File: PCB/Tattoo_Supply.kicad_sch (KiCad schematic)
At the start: 1 part

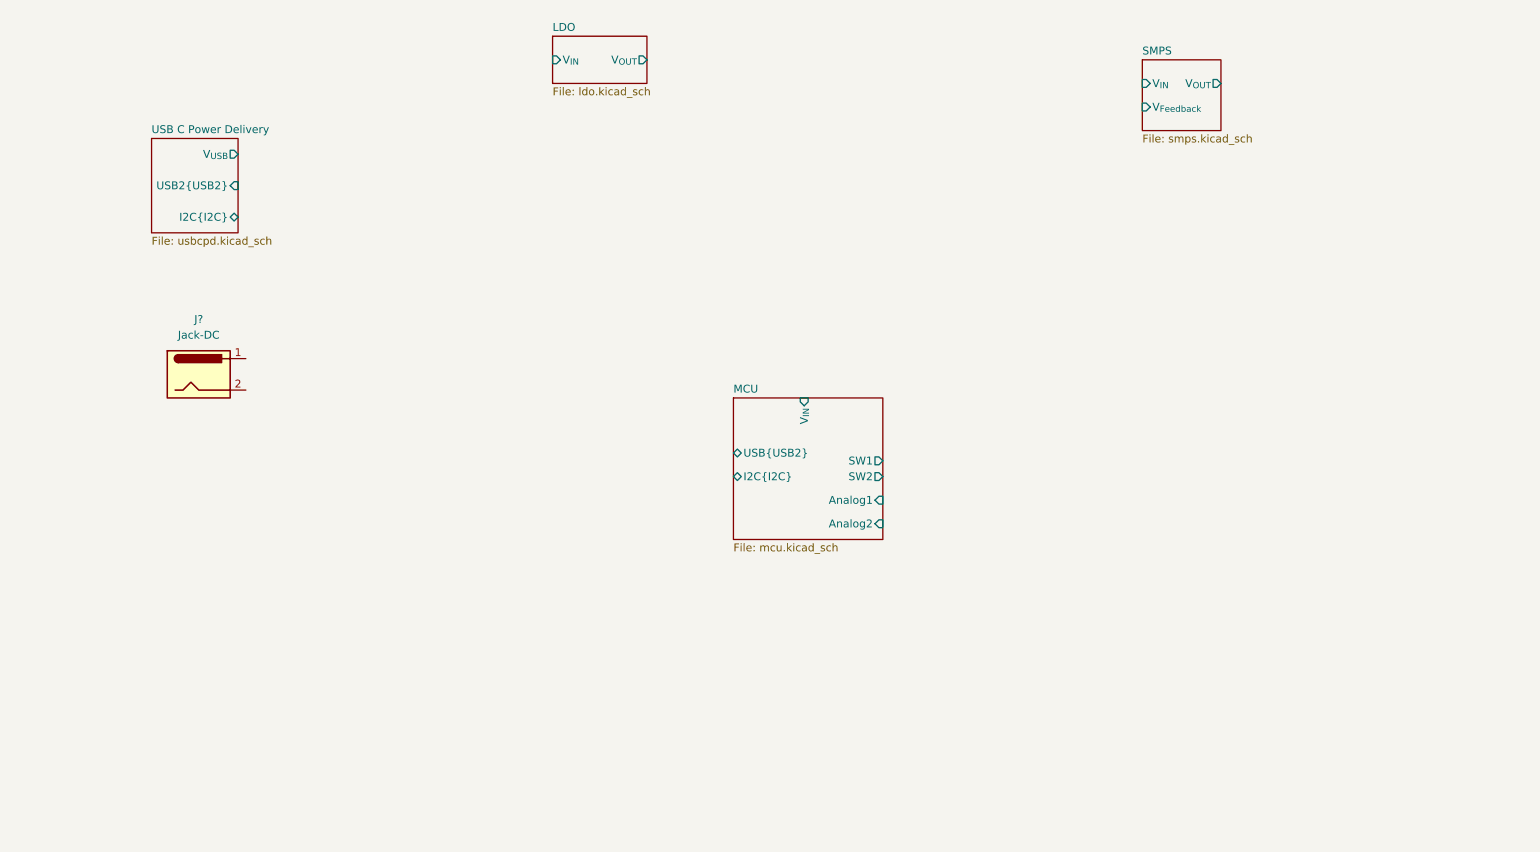
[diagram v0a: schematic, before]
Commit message: ok dcdc and power switches
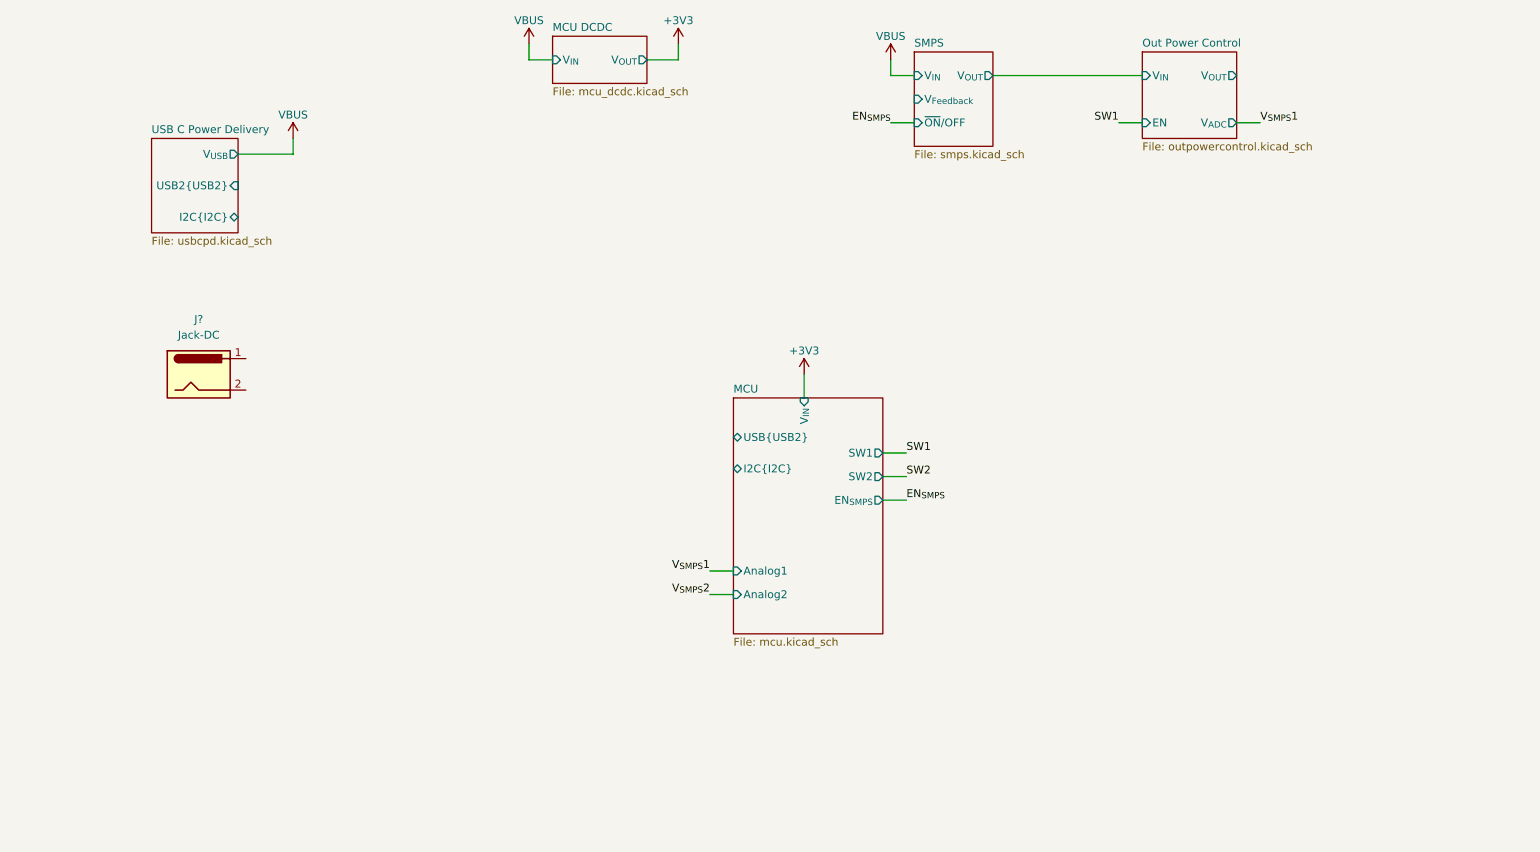
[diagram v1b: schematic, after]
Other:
- removed sheet LDO
- added sheet MCU DCDC (mcu_dcdc.kicad_sch)
- added sheet Out Power Control (outpowercontrol.kicad_sch)
- sheet MCU ports: added EN_{SMPS}; removed none
- sheet SMPS ports: added ~{ON}/OFF; removed none

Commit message: add dac
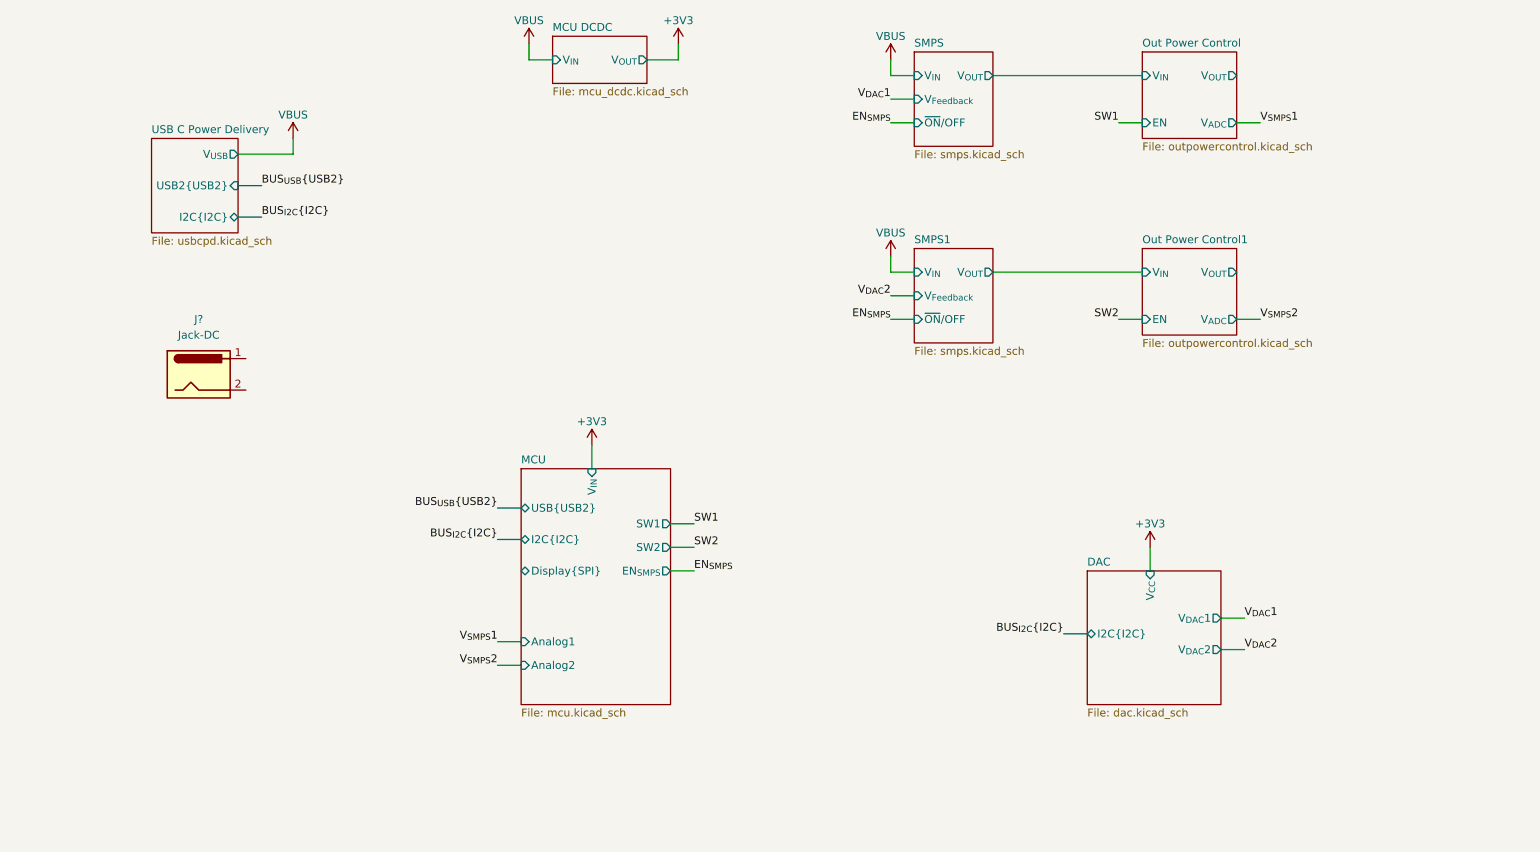
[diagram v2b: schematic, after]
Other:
- added sheet DAC (dac.kicad_sch)
- added sheet Out Power Control1 (outpowercontrol.kicad_sch)
- added sheet SMPS1 (smps.kicad_sch)
- sheet MCU ports: added Display{SPI}; removed none

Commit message: done with sch before ERC and footprints
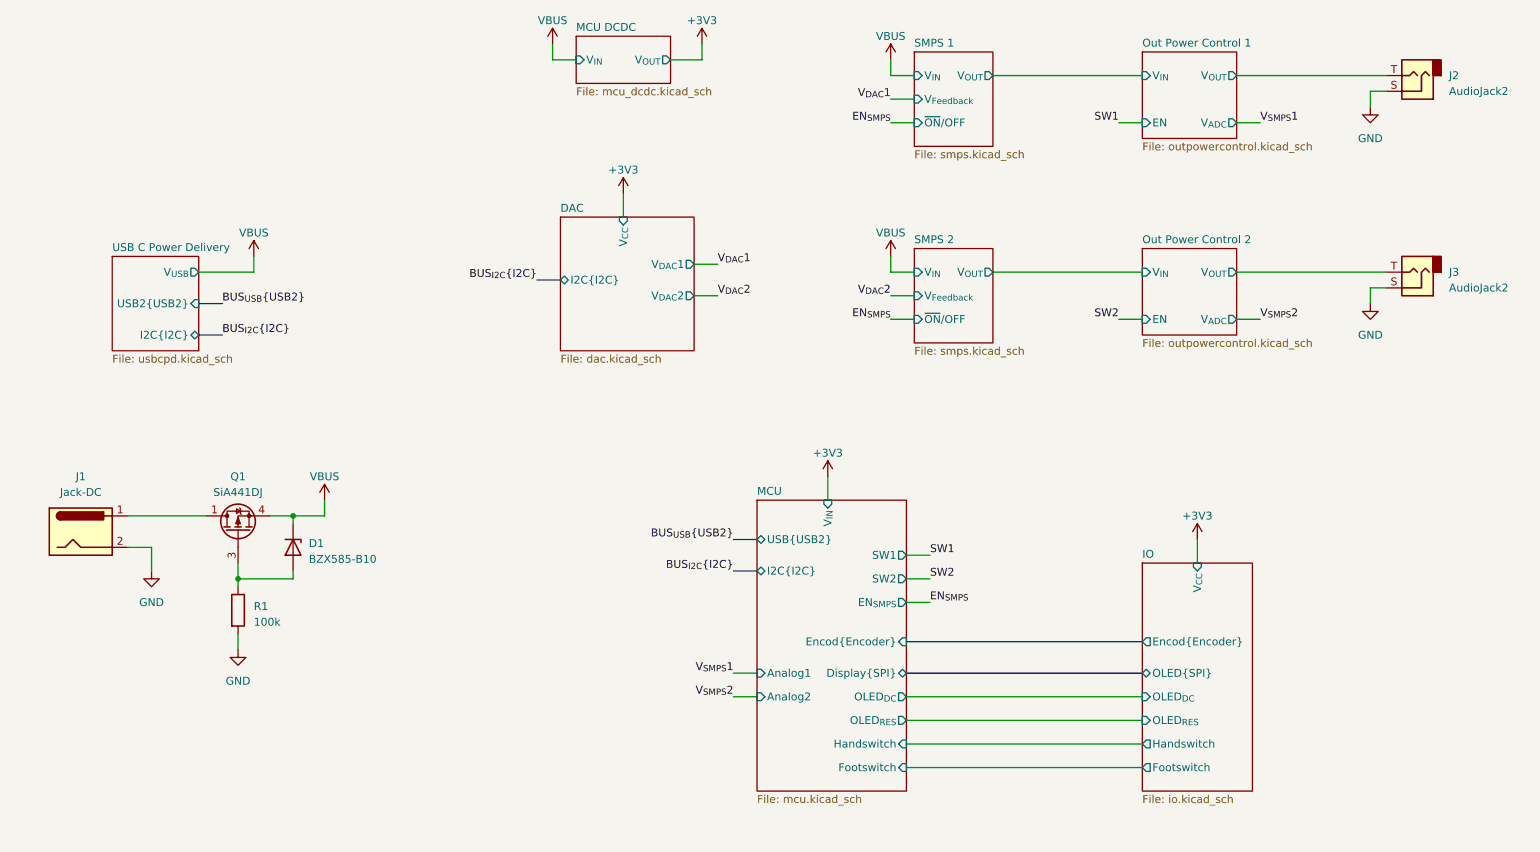
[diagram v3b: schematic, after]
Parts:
- added D1: BZX585-B10, Diode_SMD:D_SOD-523, symbol Device:D_Zener
- added J2, J3: AudioJack2, symbol Connector_Audio:AudioJack2
- added Q1: SiA441DJ, Package_TO_SOT_SMD:Vishay_PowerPAK_SC70-6L_Single, symbol Transistor_FET:SiA449DJ
- added R1: 100k, symbol Device:R
- gave numbers to parts that had none: 1
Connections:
- net Out Power Control 1/V_{OUT}: now also J2.T
- net Out Power Control 2/V_{OUT}: now also J3.T
- net VBUS: now also D1.1 (K), Q1.4 (S)
- net at J1.1: now also Q1.1 (D)
- net GND: now reaches J1.2
- net GND: now also J2.S, J3.S, R1.2
- new net: D1.2 (A), Q1.3 (G), R1.1
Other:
- sheet Out Power Control renamed Out Power Control 1
- sheet Out Power Control1 renamed Out Power Control 2
- sheet SMPS renamed SMPS 1
- sheet SMPS1 renamed SMPS 2
- added sheet IO (io.kicad_sch)
- sheet MCU ports: added Encod{Encoder}, Footswitch, Handswitch, OLED_{DC}, OLED_{RES}; removed none
- title: (none) -> Tattoo Power Supply
- moved on the sheet: J1

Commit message: begin BOM
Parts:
- D1: MPN (none) -> BZX585-B10,135; Manufacturer (none) -> Nexperia
- Q1: MPN (none) -> SIA441DJ-T1-GE3; Manufacturer (none) -> Vishay Semiconductors
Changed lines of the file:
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@@
     (rev "V1.0")
   )
-  (bus_alias "I2C" (members "SDA" "SCL"))
-  (bus_alias "Encoder" (members "DT" "CLK" "SW"))
+  (bus_alias "SPI" (members "~{CS}" "SCK" "MOSI" "MISO"))
   (bus_alias "USB2" (members "D+" "D-"))
   (bus_alias "UART" (members "Tx" "Rx"))
-  (bus_alias "SPI" (members "~{CS}" "SCK" "MOSI" "MISO"))
+  (bus_alias "Encoder" (members "DT" "CLK" "SW"))
+  (bus_alias "I2C" (members "SDA" "SCL"))
   (junction (at 60.96 124.46) (diameter 0) (color 0 0 0 0)
   )
@@
       (effects (font (size 1.27 1.27)) hide)
     )
+    (property "MPN" "" (at 251.46 43.18 0)
+      (effects (font (size 1.27 1.27)) hide)
+    )
+    (property "Manufacturer" "" (at 251.46 43.18 0)
+      (effects (font (size 1.27 1.27)) hide)
+    )
     (pin "S")
     (pin "T")
@@
       (effects (font (size 1.27 1.27)) hide)
     )
+    (property "MPN" "BZX585-B10,135" (at 69.85 119.38 0)
+      (effects (font (size 1.27 1.27)) hide)
+    )
+    (property "Manufacturer" "Nexperia" (at 69.85 119.38 0)
+      (effects (font (size 1.27 1.27)) hide)
+    )
     (pin "1")
     (pin "2")
@@
       (effects (font (size 1.27 1.27)) hide)
     )
+    (property "MPN" "" (at 251.46 74.93 0)
+      (effects (font (size 1.27 1.27)) hide)
+    )
+    (property "Manufacturer" "" (at 251.46 74.93 0)
+      (effects (font (size 1.27 1.27)) hide)
+    )
     (pin "S")
     (pin "T")
@@
       (effects (font (size 1.27 1.27)) hide)
     )
+    (property "MPN" "" (at 35.56 116.84 0)
+      (effects (font (size 1.27 1.27)) hide)
+    )
+    (property "Manufacturer" "" (at 35.56 116.84 0)
+      (effects (font (size 1.27 1.27)) hide)
+    )
     (pin "1")
     (pin "2")
@@
       (effects (font (size 1.27 1.27)) (justify left) hide)
     )
+    (property "MPN" "SIA441DJ-T1-GE3" (at 60.96 116.84 0)
+      (effects (font (size 1.27 1.27)) hide)
+    )
+    (property "Manufacturer" "Vishay Semiconductors" (at 60.96 116.84 0)
+      (effects (font (size 1.27 1.27)) hide)
+    )
     (pin "1")
     (pin "3")
@@
       (effects (font (size 1.27 1.27)) hide)
     )
+    (property "MPN" "" (at 60.96 129.54 0)
+      (effects (font (size 1.27 1.27)) hide)
+    )
+    (property "Manufacturer" "" (at 60.96 129.54 0)
+      (effects (font (size 1.27 1.27)) hide)
+    )

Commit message: Resistors ok in BOM
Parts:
- R1: footprint (none) -> Resistor_SMD:R_0603_1608Metric; MPN (none) -> ERJ-3EKF1003V; Manufacturer (none) -> Panasonic
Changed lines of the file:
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@@
     (rev "V1.0")
   )
+  (bus_alias "UART" (members "Tx" "Rx"))
+  (bus_alias "I2C" (members "SDA" "SCL"))
+  (bus_alias "Encoder" (members "DT" "CLK" "SW"))
+  (bus_alias "USB2" (members "D+" "D-"))
   (bus_alias "SPI" (members "~{CS}" "SCK" "MOSI" "MISO"))
-  (bus_alias "USB2" (members "D+" "D-"))
-  (bus_alias "UART" (members "Tx" "Rx"))
-  (bus_alias "Encoder" (members "DT" "CLK" "SW"))
-  (bus_alias "I2C" (members "SDA" "SCL"))
   (junction (at 60.96 124.46) (diameter 0) (color 0 0 0 0)
   )
@@
       (effects (font (size 1.27 1.27)) (justify left))
     )
-    (property "Footprint" "" (at 59.182 129.54 90)
+    (property "Footprint" "Resistor_SMD:R_0603_1608Metric" (at 59.182 129.54 90)
       (effects (font (size 1.27 1.27)) hide)
     )
@@
       (effects (font (size 1.27 1.27)) hide)
     )
-    (property "MPN" "" (at 60.96 129.54 0)
-      (effects (font (size 1.27 1.27)) hide)
-    )
-    (property "Manufacturer" "" (at 60.96 129.54 0)
-      (effects (font (size 1.27 1.27)) hide)
-    )
+    (property "MPN" "ERJ-3EKF1003V" (at 60.96 129.54 0)
+      (effects (font (size 1.27 1.27)) hide)
+    )
+    (property "Manufacturer" "Panasonic" (at 60.96 129.54 0)
+      (effects (font (size 1.27 1.27)) hide)
+    )

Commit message: bom almost finished
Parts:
- removed J1: Jack-DC, symbol Connector:Jack-DC
- added J1: Barrel_Jack_Switch, Connector_BarrelJack:BarrelJack_CUI_PJ-102AH_Horizontal, symbol Connector:Barrel_Jack_Switch
- J2: value AudioJack2 -> Out_{1}; MPN (none) -> MJ-63022A; Manufacturer (none) -> CUI Devices
- J3: value AudioJack2 -> Out_{2}; MPN (none) -> MJ-63022A; Manufacturer (none) -> CUI Devices
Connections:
- net GND: now also J1.2, J1.3
- net at Q1.1 (D): now also J1.1
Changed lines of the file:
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@@
     (rev "V1.0")
   )
+  (bus_alias "USB2" (members "D+" "D-"))
+  (bus_alias "SPI" (members "~{CS}" "SCK" "MOSI" "MISO"))
+  (bus_alias "Encoder" (members "DT" "CLK" "SW"))
   (bus_alias "UART" (members "Tx" "Rx"))
   (bus_alias "I2C" (members "SDA" "SCL"))
-  (bus_alias "Encoder" (members "DT" "CLK" "SW"))
-  (bus_alias "USB2" (members "D+" "D-"))
-  (bus_alias "SPI" (members "~{CS}" "SCK" "MOSI" "MISO"))
+  (junction (at 46.99 119.38) (diameter 0) (color 0 0 0 0)
+  )
   (junction (at 60.96 124.46) (diameter 0) (color 0 0 0 0)
   )
@@
     (stroke (width 0) (type default))
   )
+  (wire (pts (xy 46.99 116.84) (xy 46.99 119.38))
+    (stroke (width 0) (type default))
+  )
   (wire (pts (xy 168.91 120.65) (xy 172.72 120.65))
     (stroke (width 0) (type default))
@@
     (stroke (width 0) (type default))
   )
+  (wire (pts (xy 43.18 116.84) (xy 46.99 116.84))
+    (stroke (width 0) (type default))
+  )
   (wire (pts (xy 166.37 40.64) (xy 166.37 43.18))
     (stroke (width 0) (type default))
@@
   )
   (symbol (lib_id "Connector_Audio:AudioJack2") (at 251.46 43.18 180) (unit 1)
-    (in_bom yes) (on_board yes) (dnp no) (fields_autoplaced)
+    (in_bom yes) (on_board yes) (dnp no)
     (property "Reference" "J2" (at 256.54 43.18 0)
       (effects (font (size 1.27 1.27)) (justify right))
     )
-    (property "Value" "AudioJack2" (at 256.54 45.72 0)
+    (property "Value" "Out_{1}" (at 256.54 45.72 0)
       (effects (font (size 1.27 1.27)) (justify right))
     )
@@
       (effects (font (size 1.27 1.27)) hide)
     )
-    (property "MPN" "" (at 251.46 43.18 0)
-      (effects (font (size 1.27 1.27)) hide)
-    )
-    (property "Manufacturer" "" (at 251.46 43.18 0)
+    (property "MPN" "MJ-63022A" (at 251.46 43.18 0)
+      (effects (font (size 1.27 1.27)) hide)
+    )
+    (property "Manufacturer" "CUI Devices" (at 251.46 43.18 0)
       (effects (font (size 1.27 1.27)) hide)
     )
@@
   )
   (symbol (lib_id "Connector_Audio:AudioJack2") (at 251.46 74.93 180) (unit 1)
-    (in_bom yes) (on_board yes) (dnp no) (fields_autoplaced)
+    (in_bom yes) (on_board yes) (dnp no)
     (property "Reference" "J3" (at 256.54 74.93 0)
       (effects (font (size 1.27 1.27)) (justify right))
     )
-    (property "Value" "AudioJack2" (at 256.54 77.47 0)
+    (property "Value" "Out_{2}" (at 256.54 77.47 0)
       (effects (font (size 1.27 1.27)) (justify right))
     )
@@
       (effects (font (size 1.27 1.27)) hide)
     )
-    (property "MPN" "" (at 251.46 74.93 0)
-      (effects (font (size 1.27 1.27)) hide)
-    )
-    (property "Manufacturer" "" (at 251.46 74.93 0)
+    (property "MPN" "MJ-63022A" (at 251.46 74.93 0)
+      (effects (font (size 1.27 1.27)) hide)
+    )
+    (property "Manufacturer" "CUI Devices" (at 251.46 74.93 0)
       (effects (font (size 1.27 1.27)) hide)
     )
@@
     )
   )
-  (symbol (lib_id "Connector:Jack-DC") (at 35.56 116.84 0) (unit 1)
-    (in_bom yes) (on_board yes) (dnp no) (fields_autoplaced)
-    (property "Reference" "J1" (at 35.56 107.95 0)
-      (effects (font (size 1.27 1.27)))
-    )
-    (property "Value" "Jack-DC" (at 35.56 110.49 0)
-      (effects (font (size 1.27 1.27)))
-    )
-    (property "Footprint" "" (at 36.83 117.856 0)
+  (symbol (lib_id "power:VBUS") (at 166.37 72.39 0) (unit 1)
+    (in_bom yes) (on_board yes) (dnp no) (fields_autoplaced)
+    (property "Reference" "#PWR010" (at 166.37 76.2 0)
+      (effects (font (size 1.27 1.27)) hide)
+    )
+    (property "Value" "VBUS" (at 166.37 68.58 0)
+      (effects (font (size 1.27 1.27)))
+    )
+    (property "Footprint" "" (at 166.37 72.39 0)
+      (effects (font (size 1.27 1.27)) hide)
+    )
+    (property "Datasheet" "" (at 166.37 72.39 0)
+      (effects (font (size 1.27 1.27)) hide)
+    )
+    (pin "1")
+    (instances
+      (project "Tattoo_Supply"
+        (path "/036b57f3-323c-4da7-bad2-1c27fa1415e1"
+          (reference "#PWR010") (unit 1)
+        )
+      )
+    )
+  )
+  (symbol (lib_id "Connector:Barrel_Jack_Switch") (at 35.56 116.84 0) (unit 1)
+    (in_bom yes) (on_board yes) (dnp no) (fields_autoplaced)
+    (property "Reference" "J1" (at 35.56 109.22 0)
+      (effects (font (size 1.27 1.27)))
+    )
+    (property "Value" "Barrel_Jack_Switch" (at 35.56 111.76 0)
+      (effects (font (size 1.27 1.27)))
+    )
+    (property "Footprint" "Connector_BarrelJack:BarrelJack_CUI_PJ-102AH_Horizontal" (at 36.83 117.856 0)
       (effects (font (size 1.27 1.27)) hide)
     )
@@
       (effects (font (size 1.27 1.27)) hide)
     )
-    (property "MPN" "" (at 35.56 116.84 0)
-      (effects (font (size 1.27 1.27)) hide)
-    )
-    (property "Manufacturer" "" (at 35.56 116.84 0)
+    (property "MPN" "PJ-102A" (at 35.56 116.84 0)
+      (effects (font (size 1.27 1.27)) hide)
+    )
+    (property "Manufacturer" "CUI Devices" (at 35.56 116.84 0)
       (effects (font (size 1.27 1.27)) hide)
     )
     (pin "1")
     (pin "2")
+    (pin "3")
     (instances
       (project "Tattoo_Supply"
@@
         )
       )
-    )
-  )
-  (symbol (lib_id "power:VBUS") (at 166.37 72.39 0) (unit 1)
-    (in_bom yes) (on_board yes) (dnp no) (fields_autoplaced)
-    (property "Reference" "#PWR010" (at 166.37 76.2 0)
-      (effects (font (size 1.27 1.27)) hide)
-    )
-    (property "Value" "VBUS" (at 166.37 68.58 0)
-      (effects (font (size 1.27 1.27)))
-    )
-    (property "Footprint" "" (at 166.37 72.39 0)
-      (effects (font (size 1.27 1.27)) hide)
-    )
-    (property "Datasheet" "" (at 166.37 72.39 0)
-      (effects (font (size 1.27 1.27)) hide)
-    )
-    (pin "1")
-    (instances
-      (project "Tattoo_Supply"
-        (path "/036b57f3-323c-4da7-bad2-1c27fa1415e1"
-          (reference "#PWR010") (unit 1)
-        )
-      )
